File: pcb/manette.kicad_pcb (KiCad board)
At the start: 2 copper layers, 120 x 60 mm, 13 parts

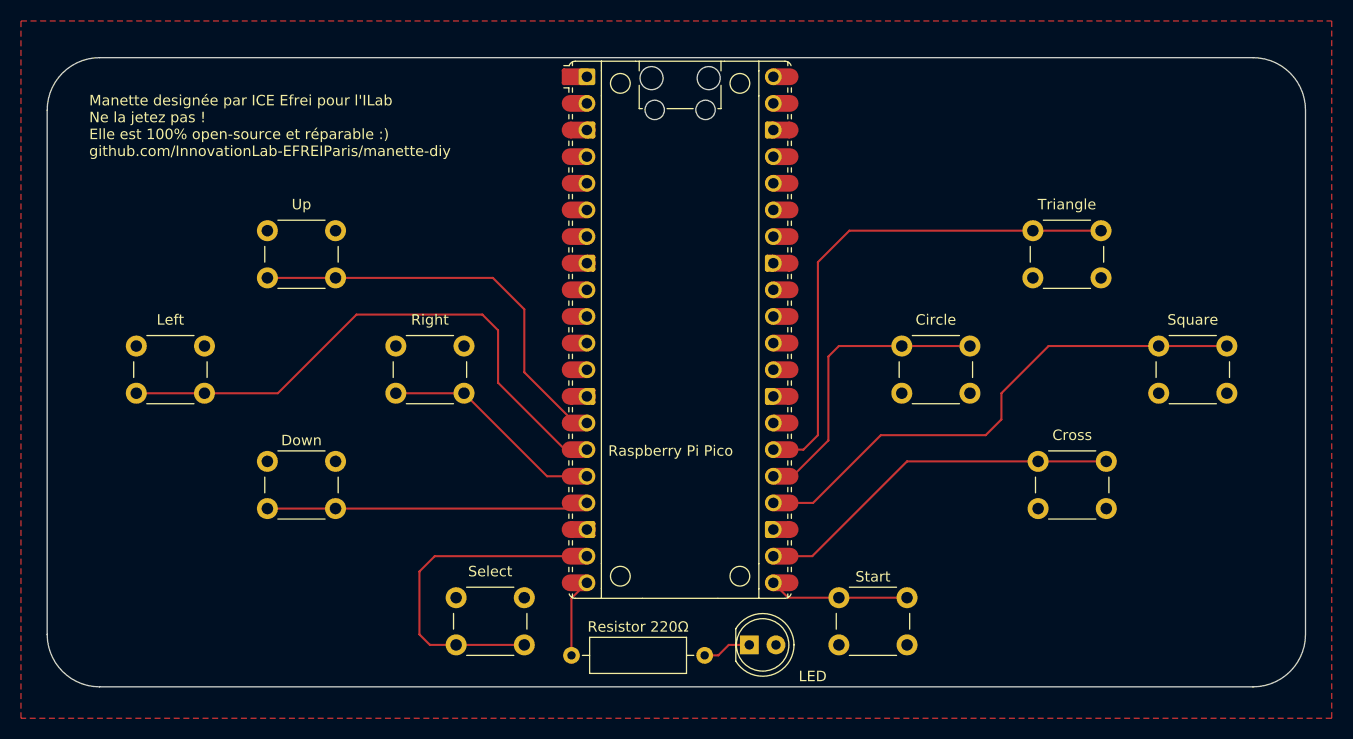
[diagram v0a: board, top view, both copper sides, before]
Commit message: switched tracks
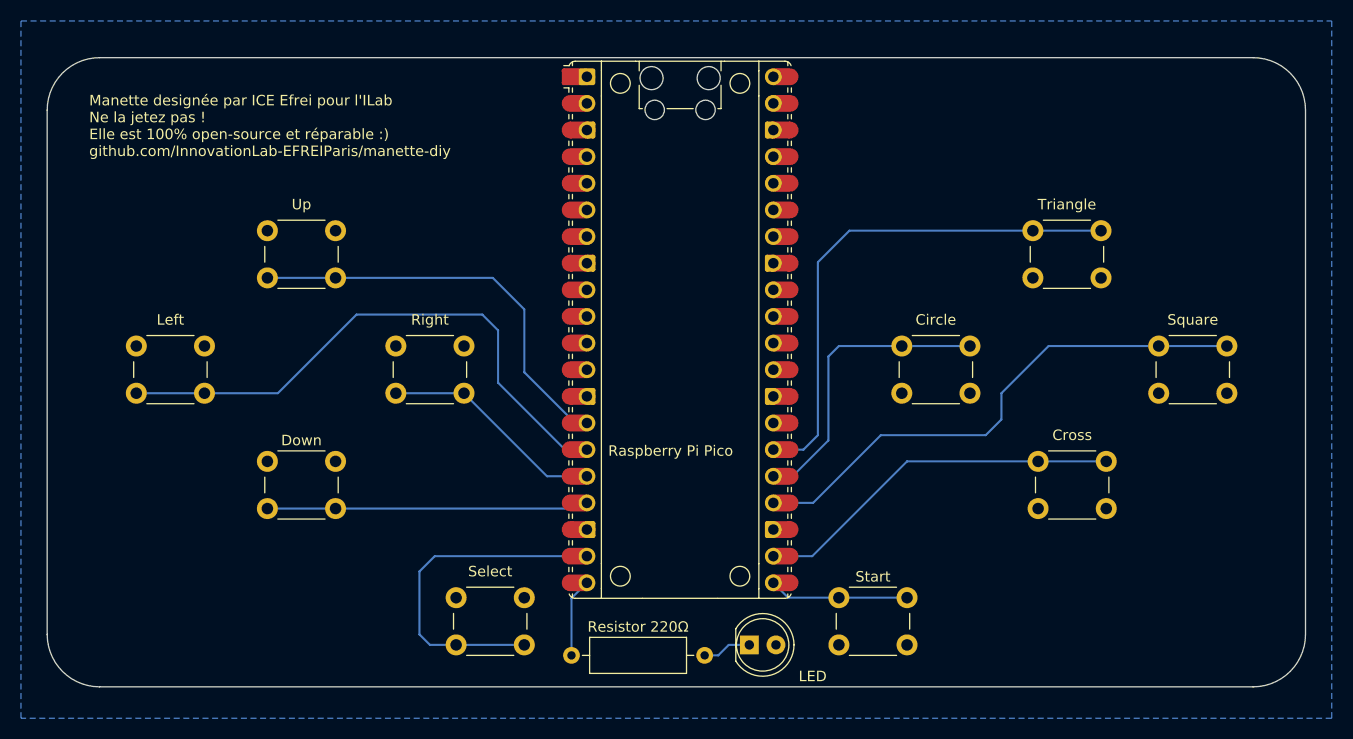
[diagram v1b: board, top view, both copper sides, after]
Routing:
- added copper zone on B.Cu, net GND
- removed copper zone on F.Cu, net GND
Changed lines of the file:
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@@
 		)
 		(group ""
-			(members "143cc3c7-45df-44b5-ace4-72eade927cba" "16da2c79-eb8e-4a21-8e91-b527a13089a7"
-				"25c9390d-390d-4039-afb9-108e6b261952" "440bb848-ac02-4900-b610-40c50773352f"
-				"5354a05f-445f-4b2a-8f72-539708840346" "689773cc-7738-4e6f-9885-86ee376b6ed1"
-				"711a541f-b910-4d0a-b400-87295cea4838" "785d6337-3c22-4947-9041-7e9dd2b0bf75"
-				"7ff7ed59-524e-4dfd-92f0-6e62341509cf" "9f82071f-5426-41bd-8bd7-7c27a9bdbd2d"
-				"bf9593fa-2abe-4d88-a106-cebdd960b699" "c529fe7f-a4fa-4845-86e7-55aa7a506082"
-				"cfcc21f1-3f6a-46f6-b471-3f7f71edcdb6" "d2316a95-3f6a-40ce-bf8f-fcebb1a97605"
-				"e0914681-2b02-426a-9042-eb2132166c6e" "efe00a95-6d29-4591-8eb3-2eb63dc863f3"
-				"f816d7c4-ff45-486c-848f-0aa424b2698a" "ff538873-a4f0-4c57-a013-57afc7312ce1"
-			)
-		)
-		(group ""
 			(members "0047d9cf-0a92-4520-bf5b-8578b474ba83" "0f79160f-419e-40cc-995c-f0fd8efd87b1"
 				"0fa63445-f260-4447-b45d-554a2485a77e" "151fa4e0-f8d6-4de4-b84b-3c63ea8936dd"
@@
 		)
 		(group ""
+			(members "143cc3c7-45df-44b5-ace4-72eade927cba" "16da2c79-eb8e-4a21-8e91-b527a13089a7"
+				"25c9390d-390d-4039-afb9-108e6b261952" "440bb848-ac02-4900-b610-40c50773352f"
+				"5354a05f-445f-4b2a-8f72-539708840346" "689773cc-7738-4e6f-9885-86ee376b6ed1"
+				"711a541f-b910-4d0a-b400-87295cea4838" "785d6337-3c22-4947-9041-7e9dd2b0bf75"
+				"7ff7ed59-524e-4dfd-92f0-6e62341509cf" "9f82071f-5426-41bd-8bd7-7c27a9bdbd2d"
+				"bf9593fa-2abe-4d88-a106-cebdd960b699" "c529fe7f-a4fa-4845-86e7-55aa7a506082"
+				"cfcc21f1-3f6a-46f6-b471-3f7f71edcdb6" "d2316a95-3f6a-40ce-bf8f-fcebb1a97605"
+				"e0914681-2b02-426a-9042-eb2132166c6e" "efe00a95-6d29-4591-8eb3-2eb63dc863f3"
+				"f816d7c4-ff45-486c-848f-0aa424b2698a" "ff538873-a4f0-4c57-a013-57afc7312ce1"
+			)
+		)
+		(group ""
 			(members "0c40cf0d-7fd3-415e-8784-ee4b7684b06b" "19d54f71-fdf9-4a42-8a6d-62d26a9023ab"
 				"1b151c32-e4c0-4c95-8df1-d50522058ef0" "28340a6f-d583-4134-84fa-2d483a5d618b"
@@
 		(end 159.25 114.92)
 		(width 0.2)
-		(layer "F.Cu")
+		(layer "B.Cu")
 		(net 8)
 	)
@@
 		(end 165.5 102.5)
 		(width 0.2)
-		(layer "F.Cu")
+		(layer "B.Cu")
 		(net 8)
 	)
@@
 		(end 178 102.5)
 		(width 0.2)
-		(layer "F.Cu")
+		(layer "B.Cu")
 		(net 8)
 	)
@@
 		(end 164.5 103.5)
 		(width 0.2)
-		(layer "F.Cu")
+		(layer "B.Cu")
 		(net 8)
 	)
@@
 		(end 161.08 114.92)
 		(width 0.2)
-		(layer "F.Cu")
+		(layer "B.Cu")
 		(net 8)
 	)
@@
 		(end 164.5 111.5)
 		(width 0.2)
-		(layer "F.Cu")
+		(layer "B.Cu")
 		(net 8)
 	)
@@
 		(end 172 126.5)
 		(width 0.2)
-		(layer "F.Cu")
+		(layer "B.Cu")
 		(net 10)
 	)
@@
 		(end 159.25 125.08)
 		(width 0.2)
-		(layer "F.Cu")
+		(layer "B.Cu")
 		(net 10)
 	)
@@
 		(end 160.67 126.5)
 		(width 0.2)
-		(layer "F.Cu")
+		(layer "B.Cu")
 		(net 10)
 	)
@@
 		(end 112 107)
 		(width 0.2)
-		(layer "F.Cu")
+		(layer "B.Cu")
 		(net 11)
 	)
@@
 		(end 139.38 112.38)
 		(width 0.2)
-		(layer "F.Cu")
+		(layer "B.Cu")
 		(net 11)
 	)
@@
 		(end 105 107)
 		(width 0.2)
-		(layer "F.Cu")
+		(layer "B.Cu")
 		(net 11)
 	)
@@
 		(end 133 101)
 		(width 0.2)
-		(layer "F.Cu")
+		(layer "B.Cu")
 		(net 11)
 	)
@@
 		(end 141.47 112.38)
 		(width 0.2)
-		(layer "F.Cu")
+		(layer "B.Cu")
 		(net 11)
 	)
@@
 		(end 133 106)
 		(width 0.2)
-		(layer "F.Cu")
+		(layer "B.Cu")
 		(net 11)
 	)
@@
 		(end 131.5 99.5)
 		(width 0.2)
-		(layer "F.Cu")
+		(layer "B.Cu")
 		(net 11)
 	)
@@
 		(end 119.5 99.5)
 		(width 0.2)
-		(layer "F.Cu")
+		(layer "B.Cu")
 		(net 11)
 	)
@@
 		(end 140.93 118)
 		(width 0.2)
-		(layer "F.Cu")
+		(layer "B.Cu")
 		(net 13)
 	)
@@
 		(end 141.47 117.46)
 		(width 0.2)
-		(layer "F.Cu")
+		(layer "B.Cu")
 		(net 13)
 	)
@@
 		(end 117.5 118)
 		(width 0.2)
-		(layer "F.Cu")
+		(layer "B.Cu")
 		(net 13)
 	)
@@
 		(end 163.04 117.46)
 		(width 0.2)
-		(layer "F.Cu")
+		(layer "B.Cu")
 		(net 15)
 	)
@@
 		(end 159.25 117.46)
 		(width 0.2)
-		(layer "F.Cu")
+		(layer "B.Cu")
 		(net 15)
 	)
@@
 		(end 169.5 111)
 		(width 0.2)
-		(layer "F.Cu")
+		(layer "B.Cu")
 		(net 15)
 	)
@@
 		(end 179.5 111)
 		(width 0.2)
-		(layer "F.Cu")
+		(layer "B.Cu")
 		(net 15)
 	)
@@
 		(end 181 109.5)
 		(width 0.2)
-		(layer "F.Cu")
+		(layer "B.Cu")
 		(net 15)
 	)
@@
 		(end 185.5 102.5)
 		(width 0.2)
-		(layer "F.Cu")
+		(layer "B.Cu")
 		(net 15)
 	)
@@
 		(end 181 107)
 		(width 0.2)
-		(layer "F.Cu")
+		(layer "B.Cu")
 		(net 15)
 	)
@@
 		(end 202.5 102.5)
 		(width 0.2)
-		(layer "F.Cu")
+		(layer "B.Cu")
 		(net 15)
 	)
@@
 		(end 126.5 131)
 		(width 0.2)
-		(layer "F.Cu")
+		(layer "B.Cu")
 		(net 21)
 	)
@@
 		(end 135.5 131)
 		(width 0.2)
-		(layer "F.Cu")
+		(layer "B.Cu")
 		(net 21)
 	)
@@
 		(end 126.96 122.54)
 		(width 0.2)
-		(layer "F.Cu")
+		(layer "B.Cu")
 		(net 21)
 	)
@@
 		(end 125.5 124)
 		(width 0.2)
-		(layer "F.Cu")
+		(layer "B.Cu")
 		(net 21)
 	)
@@
 		(end 141.47 122.54)
 		(width 0.2)
-		(layer "F.Cu")
+		(layer "B.Cu")
 		(net 21)
 	)
@@
 		(end 125.5 130)
 		(width 0.2)
-		(layer "F.Cu")
+		(layer "B.Cu")
 		(net 21)
 	)
@@
 		(end 163.5 111)
 		(width 0.2)
-		(layer "F.Cu")
+		(layer "B.Cu")
 		(net 23)
 	)
@@
 		(end 163.5 94.5)
 		(width 0.2)
-		(layer "F.Cu")
+		(layer "B.Cu")
 		(net 23)
 	)
@@
 		(end 166.5 91.5)
 		(width 0.2)
-		(layer "F.Cu")
+		(layer "B.Cu")
 		(net 23)
 	)
@@
 		(end 159.25 112.38)
 		(width 0.2)
-		(layer "F.Cu")
+		(layer "B.Cu")
 		(net 23)
 	)
@@
 		(end 162.12 112.38)
 		(width 0.2)
-		(layer "F.Cu")
+		(layer "B.Cu")
 		(net 23)
 	)
@@
 		(end 190.5 91.5)
 		(width 0.2)
-		(layer "F.Cu")
+		(layer "B.Cu")
 		(net 23)
 	)
@@
 		(end 129.75 107)
 		(width 0.2)
-		(layer "F.Cu")
+		(layer "B.Cu")
 		(net 28)
 	)
@@
 		(end 137.67 114.92)
 		(width 0.2)
-		(layer "F.Cu")
+		(layer "B.Cu")
 		(net 28)
 	)
@@
 		(end 141.47 114.92)
 		(width 0.2)
-		(layer "F.Cu")
+		(layer "B.Cu")
 		(net 28)
 	)
@@
 		(end 132.5 96)
 		(width 0.2)
-		(layer "F.Cu")
+		(layer "B.Cu")
 		(net 29)
 	)
@@
 		(end 141.47 109.84)
 		(width 0.2)
-		(layer "F.Cu")
+		(layer "B.Cu")
 		(net 29)
 	)
@@
 		(end 135.5 105)
 		(width 0.2)
-		(layer "F.Cu")
+		(layer "B.Cu")
 		(net 29)
 	)
@@
 		(end 135.5 99)
 		(width 0.2)
-		(layer "F.Cu")
+		(layer "B.Cu")
 		(net 29)
 	)
@@
 		(end 117.5 96)
 		(width 0.2)
-		(layer "F.Cu")
+		(layer "B.Cu")
 		(net 29)
 	)
@@
 		(end 140.34 109.84)
 		(width 0.2)
-		(layer "F.Cu")
+		(layer "B.Cu")
 		(net 29)
 	)
@@
 		(end 159.25 122.54)
 		(width 0.2)
-		(layer "F.Cu")
+		(layer "B.Cu")
 		(net 38)
 	)
@@
 		(end 162.96 122.54)
 		(width 0.2)
-		(layer "F.Cu")
+		(layer "B.Cu")
 		(net 38)
 	)
@@
 		(end 191 113.5)
 		(width 0.2)
-		(layer "F.Cu")
+		(layer "B.Cu")
 		(net 38)
 	)
@@
 		(end 172 113.5)
 		(width 0.2)
-		(layer "F.Cu")
+		(layer "B.Cu")
 		(net 38)
 	)
@@
 		(end 140 126.55)
 		(width 0.2)
-		(layer "F.Cu")
+		(layer "B.Cu")
 		(net 46)
 	)
@@
 		(end 141.47 125.08)
 		(width 0.2)
-		(layer "F.Cu")
+		(layer "B.Cu")
 		(net 46)
 	)
@@
 		(end 155 131)
 		(width 0.2)
-		(layer "F.Cu")
+		(layer "B.Cu")
 		(net 57)
 	)
@@
 		(end 154 132)
 		(width 0.2)
-		(layer "F.Cu")
+		(layer "B.Cu")
 		(net 57)
 	)
@@
 		(end 156.96 131)
 		(width 0.2)
-		(layer "F.Cu")
+		(layer "B.Cu")
 		(net 57)
 	)
@@
 		(net 12)
 		(net_name "GND")
-		(layer "F.Cu")
+		(layer "B.Cu")
 		(hatch edge 0.5)
 		(connect_pads

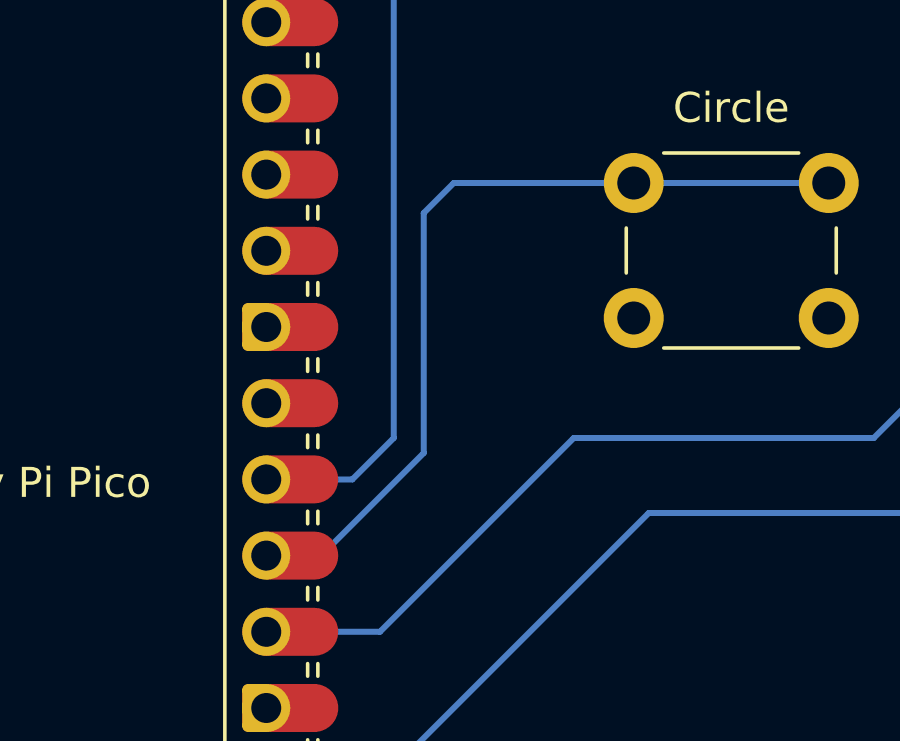
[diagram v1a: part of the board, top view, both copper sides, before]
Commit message: small routing fix for more grounding
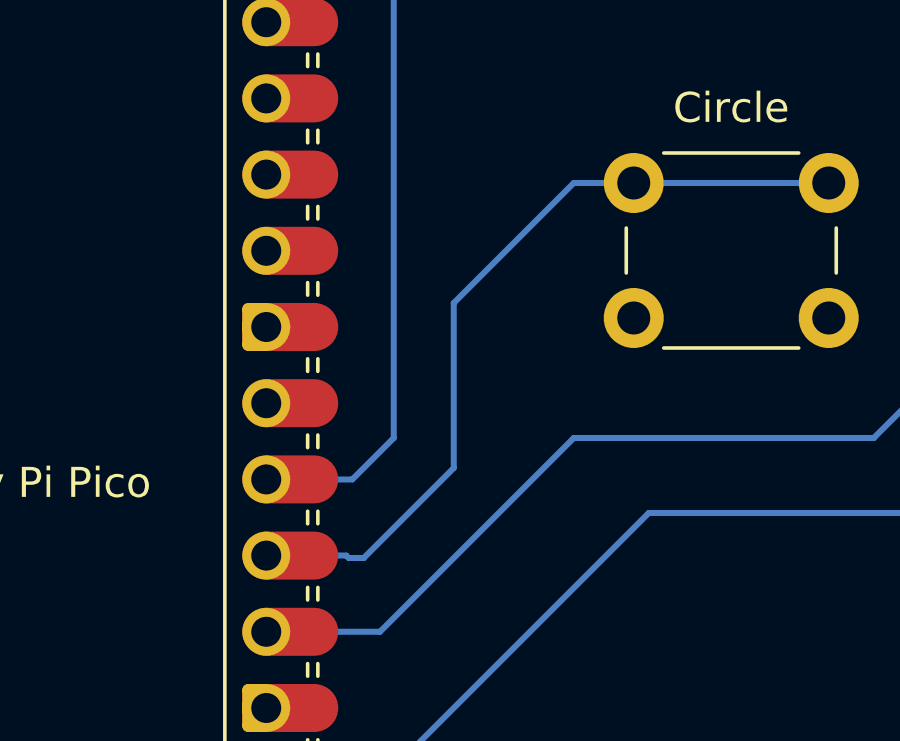
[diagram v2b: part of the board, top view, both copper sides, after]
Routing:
- net Net-(A1-GPIO19): track 28.6 -> 27.2 mm
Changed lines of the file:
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@@
 	)
 	(segment
-		(start 161.08 114.92)
+		(start 161.92 114.92)
 		(end 159.25 114.92)
 		(width 0.2)
@@
 	)
 	(segment
-		(start 171.5 102.5)
-		(end 165.5 102.5)
+		(start 165.5 106.5)
+		(end 165.5 112)
+		(width 0.2)
+		(layer "B.Cu")
+		(net 8)
+	)
+	(segment
+		(start 162 115)
+		(end 161.92 114.92)
+		(width 0.2)
+		(layer "B.Cu")
+		(net 8)
+	)
+	(segment
+		(start 169.5 102.5)
+		(end 165.5 106.5)
 		(width 0.2)
 		(layer "B.Cu")
@@
 	)
 	(segment
-		(start 165.5 102.5)
-		(end 164.5 103.5)
+		(start 162.5 115)
+		(end 162 115)
 		(width 0.2)
 		(layer "B.Cu")
@@
 	)
 	(segment
-		(start 164.5 111.5)
-		(end 161.08 114.92)
+		(start 171.5 102.5)
+		(end 169.5 102.5)
 		(width 0.2)
 		(layer "B.Cu")
@@
 	)
 	(segment
-		(start 164.5 103.5)
-		(end 164.5 111.5)
+		(start 165.5 112)
+		(end 162.5 115)
 		(width 0.2)
 		(layer "B.Cu")

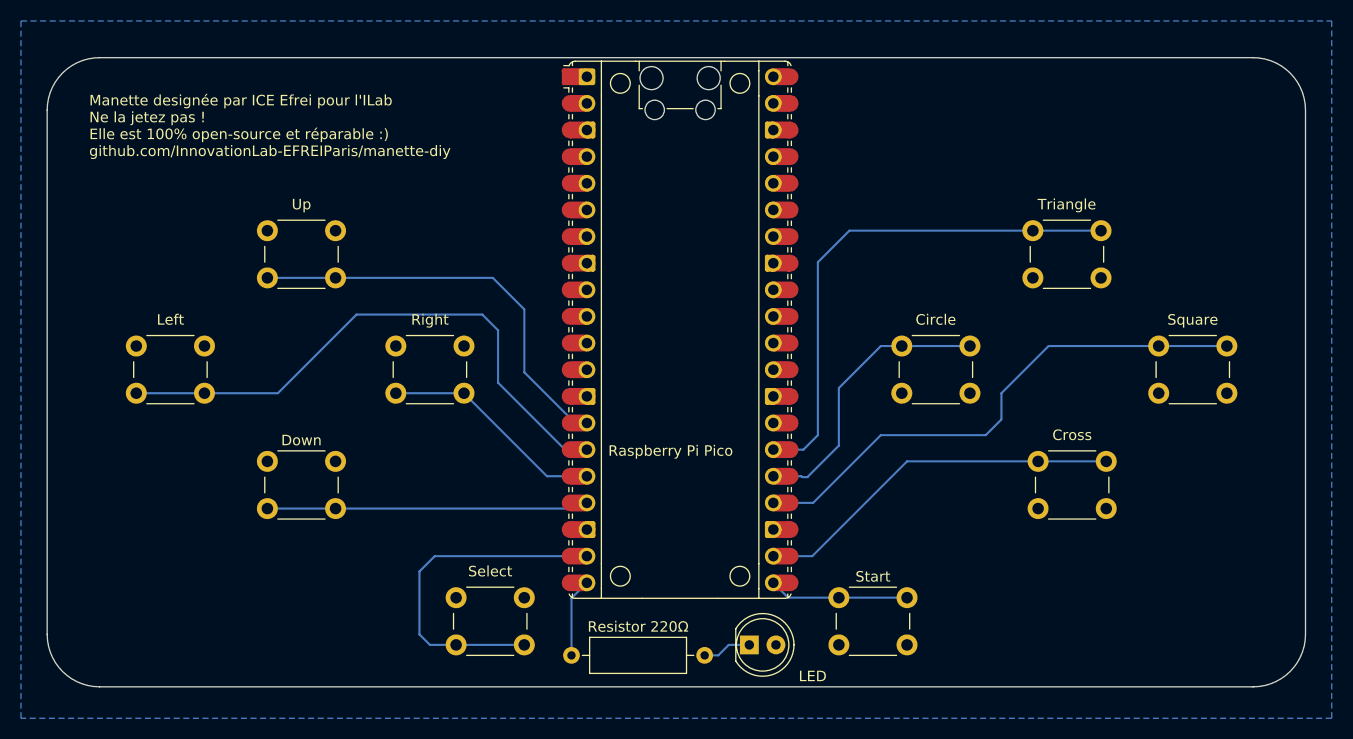
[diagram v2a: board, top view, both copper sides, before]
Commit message: updated PCB for smaller controllers
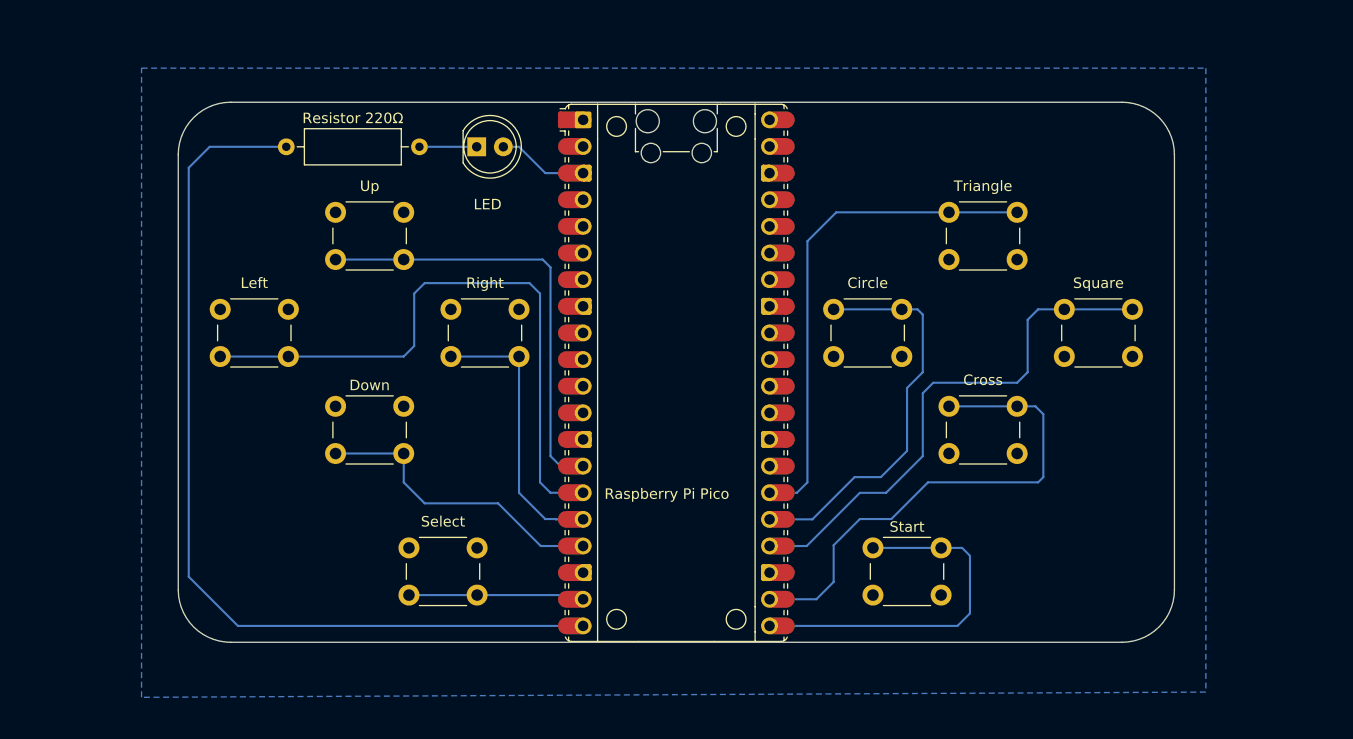
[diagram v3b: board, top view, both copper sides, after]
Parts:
- moved Resistor 220Ω 55.6 mm to (112.8, 83.5)
- moved LED 54.2 mm to (131.0, 83.5)
- moved Cross 9.99 mm to (176.0, 108.2)
- moved Square 9.66 mm to (187.0, 99.0)
- moved Left 8.73 mm to (106.5, 99.0)
- moved Down 8.36 mm to (117.5, 108.2)
- moved Triangle 8.19 mm to (176.0, 89.8)
- moved Circle 7.38 mm to (165.0, 99.0)
- moved Up 6.73 mm to (117.5, 89.8)
- moved Select 6.54 mm to (124.5, 121.8)
- moved Right 6.31 mm to (128.5, 99.0)
- moved Start 5.76 mm to (168.8, 121.8)
- moved Raspberry Pi Pico 4.13 mm to (150.0, 105.1)
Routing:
- net Net-(A1-GPIO15): track 7.53 -> 88.7 mm
- net Net-(A1-GPIO16): track 13.3 -> 34.7 mm
- net Net-(A1-GPIO14): track 33.0 -> 16.8 mm
- net Net-(A1-GPIO17): track 35.5 -> 48.3 mm
- net Net-(A1-GPIO19): track 27.2 -> 38.1 mm
- net GND: track 0.00 -> 8.65 mm
- net Net-(A1-GPIO12): track 21.5 -> 26.7 mm
- net Net-(A1-GPIO11): track 54.3 -> 59.3 mm
- net Net-(A1-GPIO10): track 39.7 -> 42.3 mm
- net Net-(A1-GPIO13): track 30.7 -> 28.9 mm
- net Net-(A1-GPIO20): track 49.6 -> 48.2 mm
- net Net-(D1-K): track 4.67 -> 5.46 mm
- net Net-(A1-GPIO18): track 50.9 -> 50.4 mm
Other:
- board size 120 x 60 mm -> 95 x 51.5 mm
- board text removed: "Manette designée par ICE Efrei pour l'ILab Ne la jetez pas ! Elle est 100% open-source et réparable :) github.com/InnovationLab-EFREIParis/manette-diy"
